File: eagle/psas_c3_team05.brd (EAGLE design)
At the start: 100 x 71.2 mm, 81 parts, among them IC1 CP2102, Q1 32 MHz, U1 MIC5219 3.3V, U2 MCP73871

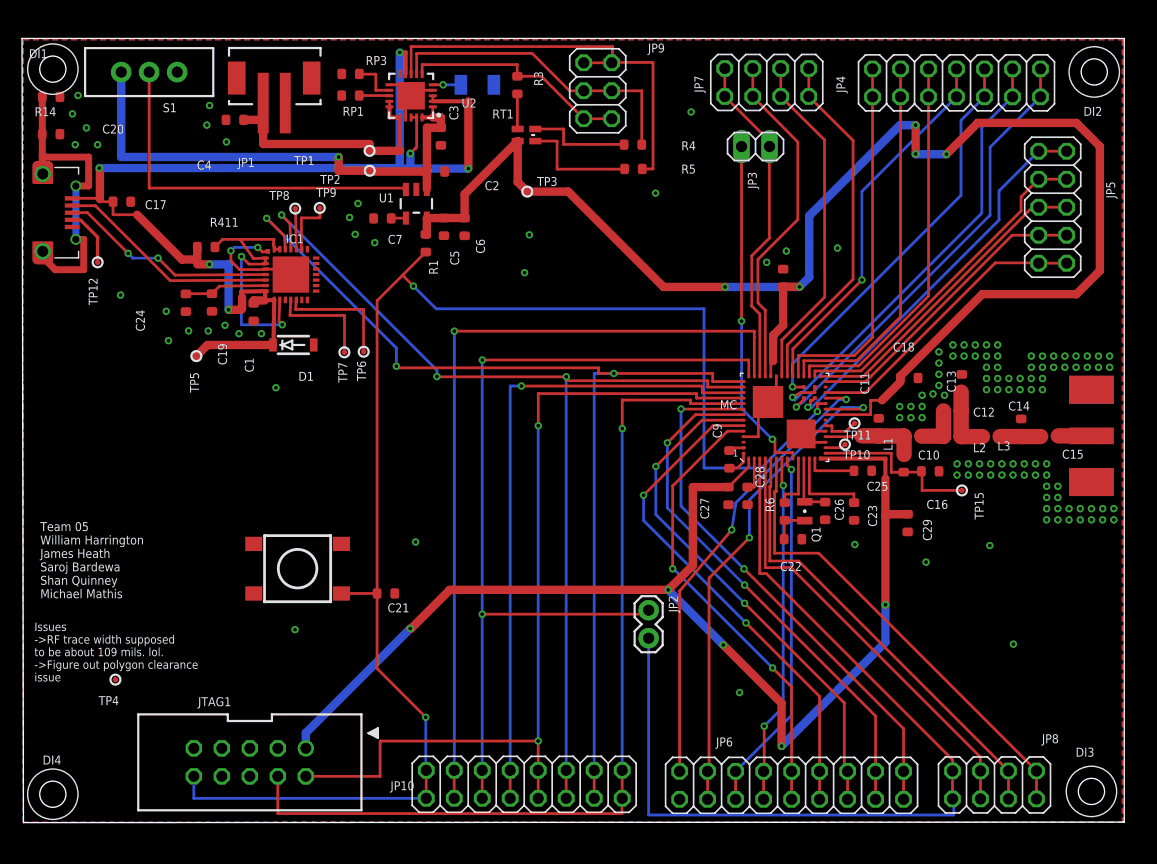
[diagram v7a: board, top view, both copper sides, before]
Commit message: Fixed some wires that were moved
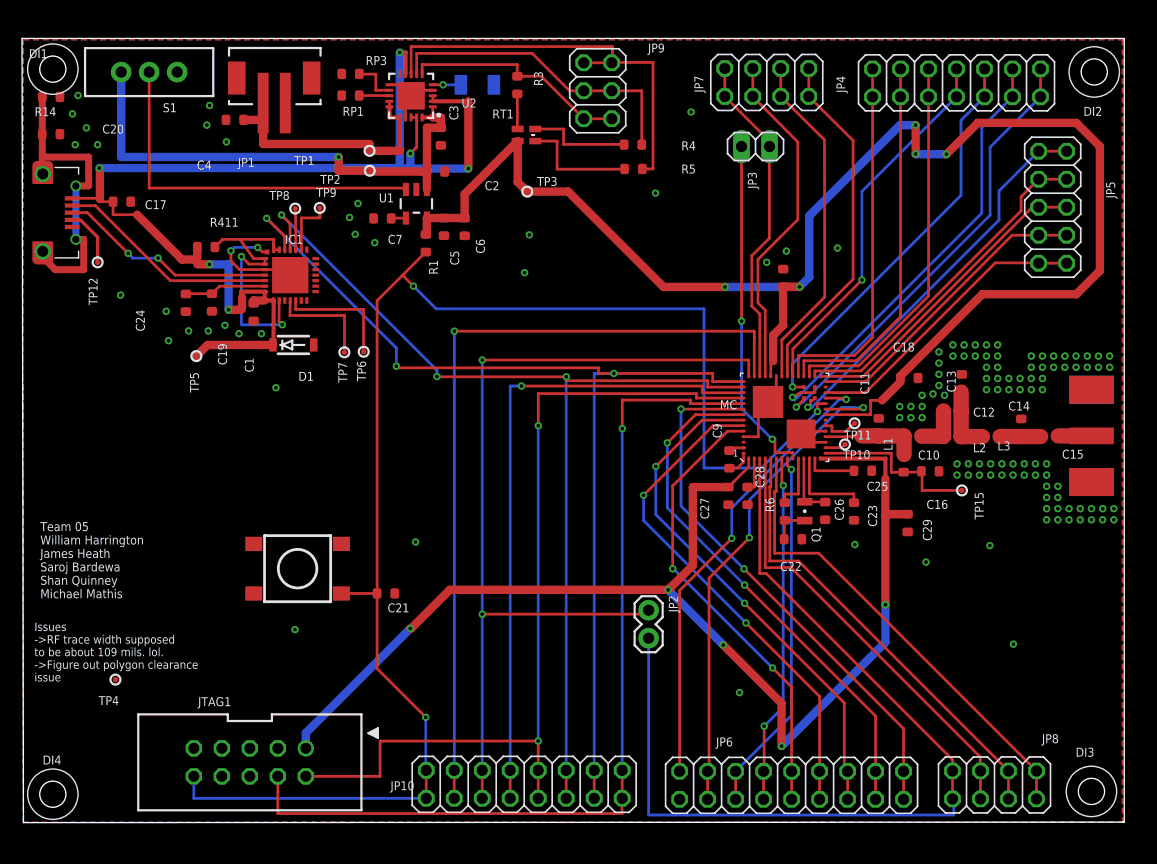
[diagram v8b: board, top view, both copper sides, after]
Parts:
- moved IC1 0.07 mm to (24.3, 49.6)
